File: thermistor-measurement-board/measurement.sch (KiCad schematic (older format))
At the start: 50 parts, among them P301 MEASURE, U301 MAX4208, U302 MAX4209, U303 MAX14661, U304 MCP3911A0-E/ML, X1 ≤ 20Mz

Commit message: some schematic review and a new TODO list
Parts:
- C307, C308: Note DNP -> (none)
- R301, R302: value R -> 660k; Note DNP -> (none)
- R311, R312: value 0 -> 100k
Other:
- note added: "Setting REFIN to about 0.4V by default. This puts it\nhigh enough to ensure REF is driven, but not too high\nfor the ADC's input range.\n"
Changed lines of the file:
@@
 P 4500 1950
 F 0 "R311" V 4580 1950 50  0000 C CNN
-F 1 "0" V 4500 1950 50  0000 C CNN
+F 1 "100k" V 4500 1950 50  0000 C CNN
 F 2 "Resistors_SMD:R_0402" V 4430 1950 50  0001 C CNN
 F 3 "" H 4500 1950 50  0000 C CNN
@@
 P 4500 950
 F 0 "R301" V 4580 950 50  0000 C CNN
-F 1 "R" V 4500 950 50  0000 C CNN
+F 1 "660k" V 4500 950 50  0000 C CNN
 F 2 "Resistors_SMD:R_0402" V 4430 950 50  0001 C CNN
 F 3 "" H 4500 950 50  0000 C CNN
-F 4 "DNP" V 4400 950 60  0000 C CNN "Note"
 	1    4500 950
 	1    0    0    -1
@@
 F 2 "Capacitors_SMD:C_0402" H 4800 1950 50  0001 C CNN
 F 3 "" H 4800 1950 50  0000 C CNN
-F 4 "DNP" H 4900 1800 60  0000 C CNN "Note"
 	1    4800 1950
 	1    0    0    -1
@@
 P 9700 1950
 F 0 "R312" V 9780 1950 50  0000 C CNN
-F 1 "0" V 9700 1950 50  0000 C CNN
+F 1 "100k" V 9700 1950 50  0000 C CNN
 F 2 "Resistors_SMD:R_0402" V 9630 1950 50  0001 C CNN
 F 3 "" H 9700 1950 50  0000 C CNN
@@
 F 2 "Capacitors_SMD:C_0402" H 10000 1950 50  0001 C CNN
 F 3 "" H 10000 1950 50  0000 C CNN
-F 4 "DNP" H 10100 1800 60  0000 C CNN "Note"
 	1    10000 1950
 	1    0    0    -1
@@
 P 9700 950
 F 0 "R302" V 9780 950 50  0000 C CNN
-F 1 "R" V 9700 950 50  0000 C CNN
+F 1 "660k" V 9700 950 50  0000 C CNN
 F 2 "Resistors_SMD:R_0402" V 9630 950 50  0001 C CNN
 F 3 "" H 9700 950 50  0000 C CNN
-F 4 "DNP" V 9600 950 60  0000 C CNN "Note"
 	1    9700 950
 	1    0    0    -1
@@
 	3500 2000 3500 1500
 Connection ~ 3500 1500
+Text Notes 6950 2700 0    60   ~ 0
+Setting REFIN to about 0.4V by default. This puts it\nhigh enough to ensure REF is driven, but not too high\nfor the ADC's input range.\n
+Wire Notes Line
+	9150 2350 9600 1400
 $EndSCHEMATC

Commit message: took care of a few board review tasks
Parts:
- added C322: 0.1u, Capacitors_SMD:C_0402, symbol CP1_Small
- added R324: 0, Resistors_SMD:R_0603, symbol R
- C307, C308: Note (none) -> isolation ≫ 1 Mohm
- R301, R302: value 660k -> 6.6M
- R311, R312: value 100k -> 1M
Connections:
- net GNDA: now also R324.1; no longer U304.7 (REFIN-)
- net OUT_B+: now also U304.4 (CH1+); no longer U304.3 (CH1-)
- net OUT_B-: now also U304.3 (CH1-)
- net ADC_REF+: now reaches C317.1, U304.6 (REFIN+/OUT)
- net ADC_REF+: now also C322.1
- new net ADC_REF-: C322.2, R324.2, U304.7 (REFIN-)
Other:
- note added: "Setting REFIN to about 0.4V by default. This puts it\nhigh enough to ensure REF is driven, but not too high\nfor the ADC's input range.\noptionally, only stuff pull-up side of these dividers\nand use an ADC to set REFIN when enabling"
- note removed: "Setting REFIN to about 0.4V by default. This puts it\nhigh enough to ensure REF is driven, but not too high\nfor the ADC's input range.\n"
- moved on the sheet: C317

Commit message: reviewed footprints
they were all more or less correct, but i massaged a couple to closer match Maxim's recommended land patterns
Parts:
- U303: footprint Housings_DFN_QFN:QFN-28-1EP_4x4mm_Pitch0.4mm -> project:Maxim_90-0035
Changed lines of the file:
@@
 F 0 "U303" H 8750 4600 50  0000 C CNN
 F 1 "MAX14661" H 8750 4800 50  0000 C CNN
-F 2 "Housings_DFN_QFN:QFN-28-1EP_4x4mm_Pitch0.4mm" H 8750 4700 50  0001 C CNN
+F 2 "project:Maxim_90-0035" H 8750 4700 50  0001 C CNN
 F 3 "Beyond-the-rail 16:2 multiplexer" H 8750 4500 50  0001 C CNN
 	1    8750 4700

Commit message: lots of design review and related fixes/improvements
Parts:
- added C323, C324: 100p, Capacitors_SMD:C_0402, symbol CP1_Small
- added D301, D302, D303, D304: 1.8V, Diodes_SMD:SOD-123, symbol ZENERsmall
- added R325, R326: 0, Resistors_SMD:R_0603, symbol R
- C322: value 0.1u -> 100p
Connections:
- net GNDA: now also D301.2 (A), D302.2 (A), D303.2 (A), D304.2 (A)
- net OUT_A+: now also C323.2, D302.1 (K)
- net OUT_A-: now also C323.1, D304.1 (K)
- net OUT_B+: now also D301.1 (K), R325.1; no longer U304.4 (CH1+)
- net OUT_B-: now also D303.1 (K), R326.1; no longer U304.3 (CH1-)
- new net: C324.1, R326.2, U304.3 (CH1-)
- new net: C324.2, R325.2, U304.4 (CH1+)
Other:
- moved on the sheet: C301, C302, C303, C304, C305, C306, C307, C308, C320, C321, R301, R302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

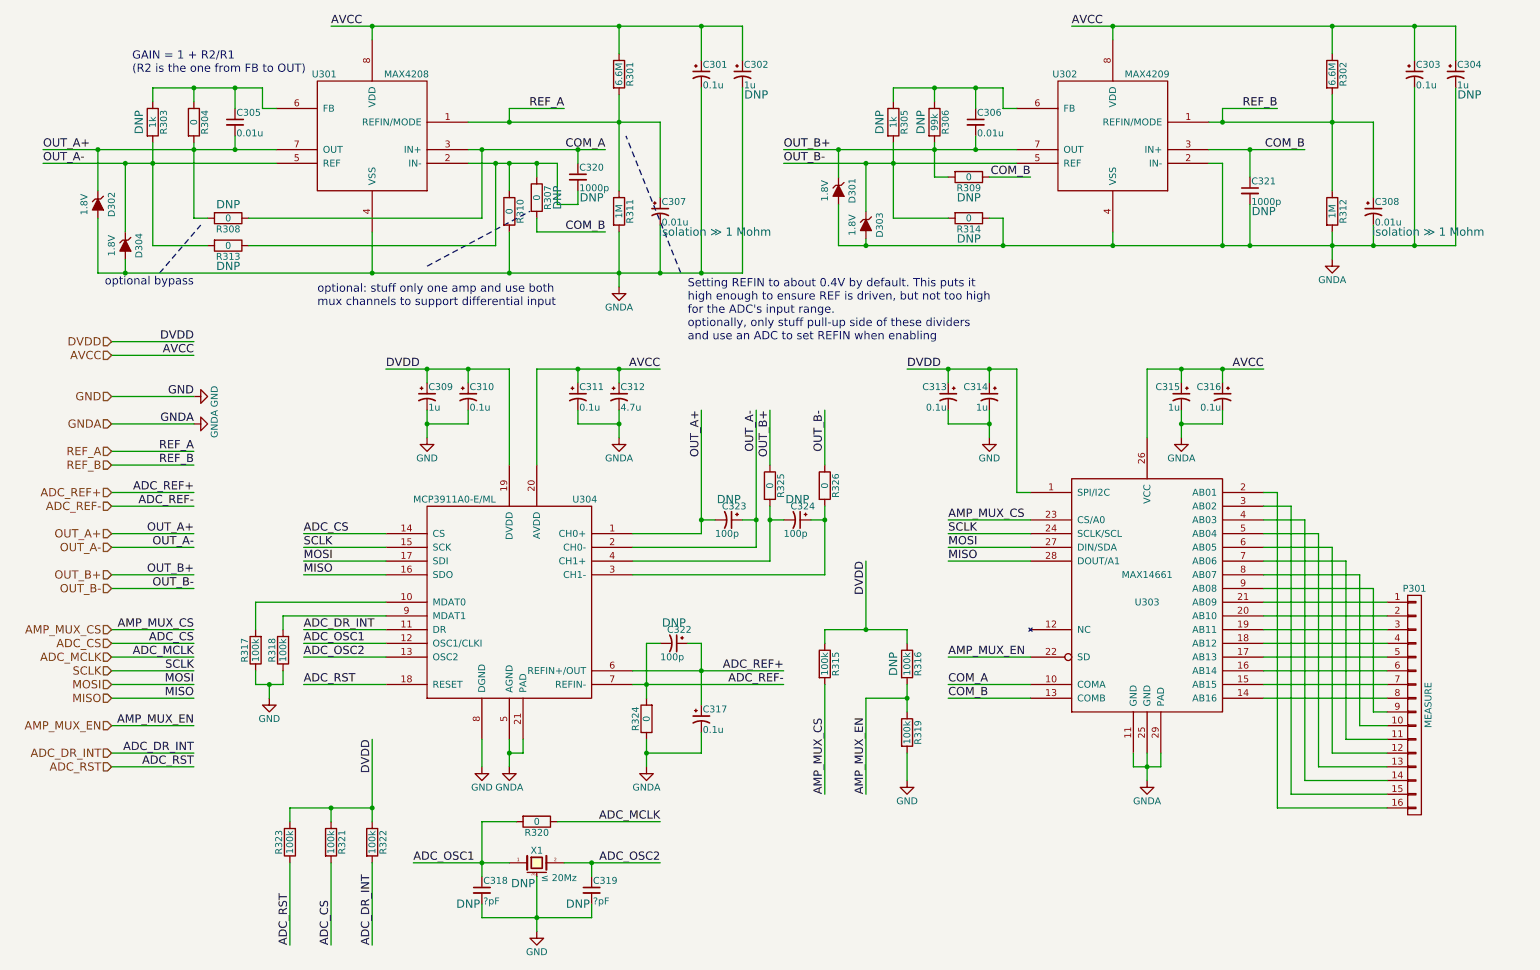
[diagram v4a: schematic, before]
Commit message: read a million instrument amp datasheets and found one that should work nicely for low gain.
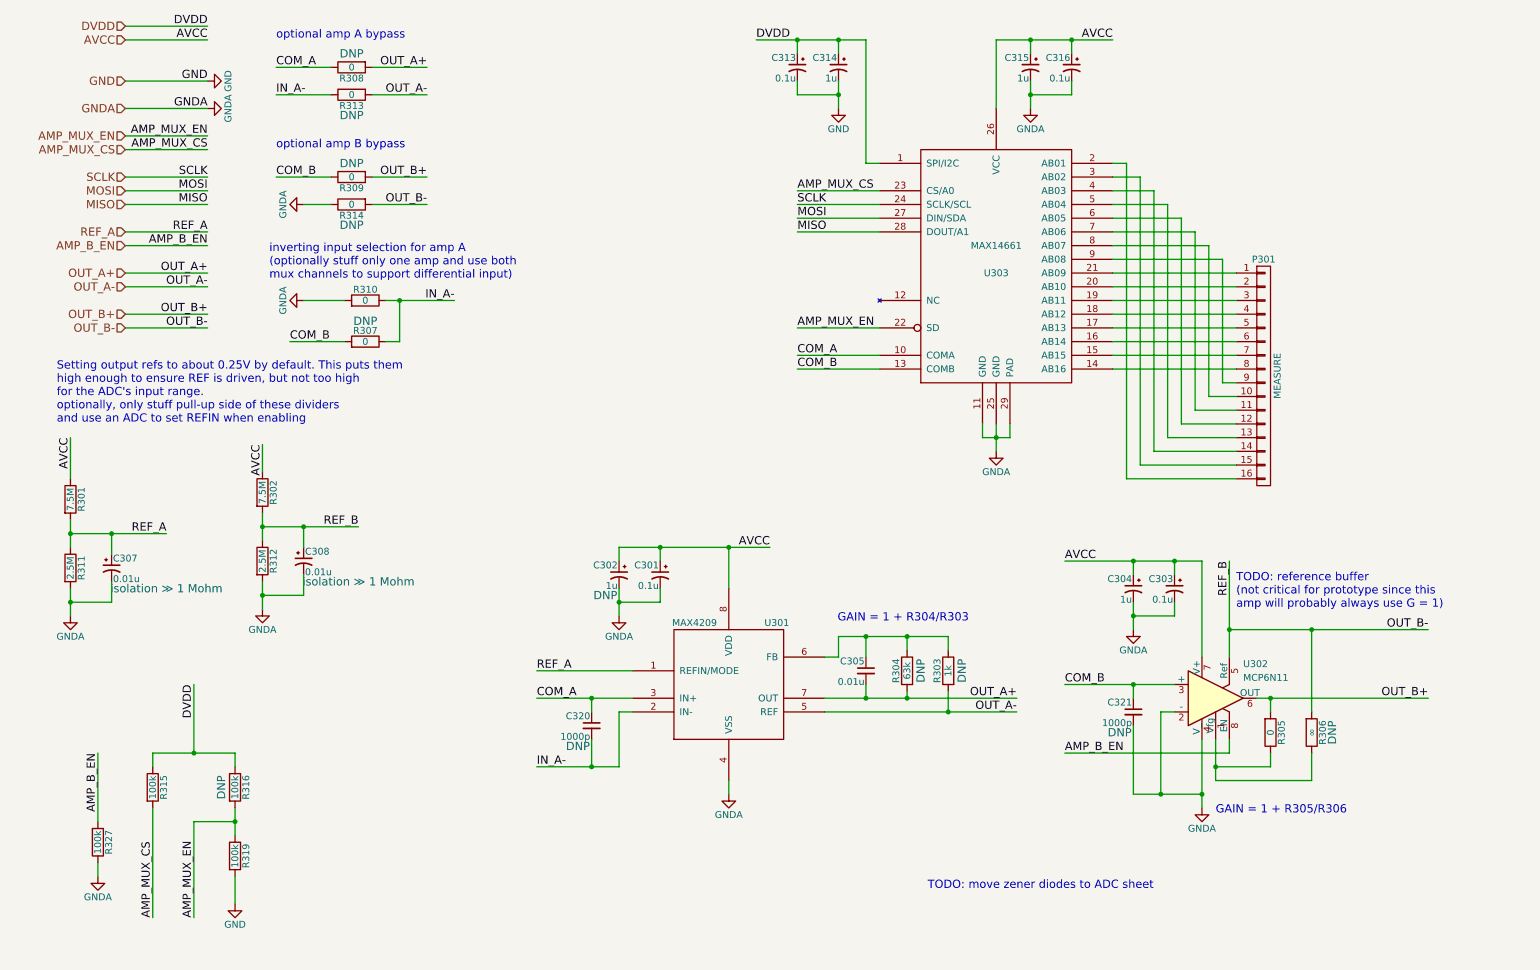
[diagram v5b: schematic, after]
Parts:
- removed C306: 0.01u, Capacitors_SMD:C_0402, symbol C_Small
- removed C309: 1u, Capacitors_SMD:C_0603, symbol CP1_Small
- removed C310, C311, C317: 0.1u, Capacitors_SMD:C_0402, symbol CP1_Small
- removed C312: 4.7u, Capacitors_SMD:C_0805, symbol CP1_Small
- removed C318, C319: ?pF, Capacitors_SMD:C_0402, symbol C_Small
- removed C322, C323, C324: 100p, Capacitors_SMD:C_0402, symbol CP1_Small
- removed D301, D302, D303, D304: 1.8V, Diodes_SMD:SOD-123, symbol ZENERsmall
- removed R317, R318, R321, R322, R323: 100k, Resistors_SMD:R_0603, symbol R
- removed R320, R324, R325, R326: 0, Resistors_SMD:R_0603, symbol R
- removed U302: MAX4209, Housings_SSOP:MSOP-8_3x3mm_Pitch0.65mm, symbol MAX3208
- removed U304: MCP3911A0-E/ML, Housings_DFN_QFN:QFN-20-1EP_4x4mm_Pitch0.5mm, symbol MCP3911A0-E/ML
- removed X1: ≤ 20Mz, Crystals:crystal_FA238-TSX3225, symbol CRYSTAL_SMD
- added R327: 100k, Resistors_SMD:R_0603, symbol R
- added U302: MCP6N11, Housings_SOIC:SOIC-8_3.9x4.9mm_Pitch1.27mm, symbol MCP6N11
- C304: Note DNP -> (none)
- R301, R302: value 6.6M -> 7.5M
- R304: value 0 -> 63k; Note (none) -> DNP
- R305: value 1k -> 0; Note DNP -> (none)
- R306: value 99k -> ∞
- R309, R314: footprint Resistors_SMD:R_0402 -> Resistors_SMD:R_0603
- R311, R312: value 1M -> 2.5M
- U301: value MAX4208 -> MAX4209
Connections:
- net REF_B is gone; now on net OUT_B-: C308.1, R302.2, R312.1
- net AVCC: now also U302.7 (V+)
- net COM_B: now also U302.3 (+)
- net GNDA: now also R327.1, U302.2 (-), U302.4 (V_)
- net OUT_B+: now also R305.2, U302.6 (OUT); no longer R306.2
- net OUT_B-: now also R306.2, U302.5 (Ref); no longer R305.2
- net IN_A-: now reaches C320.2, R307.1, R310.1, R313.1, U301.2 (IN-)
- net at R305.1, R306.1: now also U302.1 (Vfg)
- new net AMP_B_EN: R327.2, U302.8 (EN)
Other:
- note added: "GAIN = 1 + R304/R303\n"
- note added: "GAIN = 1 + R305/R306"
- note added: "Setting output refs to about 0.25V by default. This puts them\nhigh enough to ensure REF is driven, but not too high\nfor the ADC's input range.\noptionally, only stuff pull-up side of these dividers\nand use an ADC to set REFIN when enabling"
- note added: "TODO: move zener diodes to ADC sheet"
- note added: "TODO: reference buffer\n(not critical for prototype since this\namp will probably always use G = 1)"
- note added: "inverting input selection for amp A\n(optionally stuff only one amp and use both\nmux channels to support differential input)"
- note added: "optional amp A bypass"
- note added: "optional amp B bypass\n"
- note removed: "GAIN = 1 + R2/R1\n(R2 is the one from FB to OUT)"
- note removed: "Setting REFIN to about 0.4V by default. This puts it\nhigh enough to ensure REF is driven, but not too high\nfor the ADC's input range.\noptionally, only stuff pull-up side of these dividers\nand use an ADC to set REFIN when enabling"
- note removed: "optional bypass"
- note removed: "optional: stuff only one amp and use both\nmux channels to support differential input"
- moved on the sheet: C301, C302, C303, C304, C305, C307, C308, C313, C314, C315, C316, C320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

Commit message: reviewed new inamp schematic
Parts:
- R327: value 100k -> 1M
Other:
- note added: "TODO: input voltage/current limiting\n(maybe on a future version)"
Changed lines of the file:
@@
 P 1100 6550
 F 0 "R327" V 1180 6550 50  0000 C CNN
-F 1 "100k" V 1100 6550 50  0000 C CNN
+F 1 "1M" V 1100 6550 50  0000 C CNN
 F 2 "Resistors_SMD:R_0603" V 1030 6550 50  0001 C CNN
 F 3 "" H 1100 6550 50  0000 C CNN
@@
 Wire Wire Line
 	5200 4500 5200 4400
+Text Notes 8200 4350 0    60   ~ 0
+TODO: input voltage/current limiting\n(maybe on a future version)
 $EndSCHEMATC

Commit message: a few minor tweaks to thermistor board
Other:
- note removed: "TODO: move zener diodes to ADC sheet"
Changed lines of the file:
@@
 Text Label 1900 2200 2    60   ~ 0
 AMP_B_EN
-Text Notes 7150 6900 0    60   ~ 0
-TODO: move zener diodes to ADC sheet
 $Comp
 L GNDA #PWR031
